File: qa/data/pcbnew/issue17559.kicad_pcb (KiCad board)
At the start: 2 copper layers, 110.5 x 93.7 mm, 6 parts, among them IC5 AD8418AWBRZ, IC6 AD8418AWBRZ

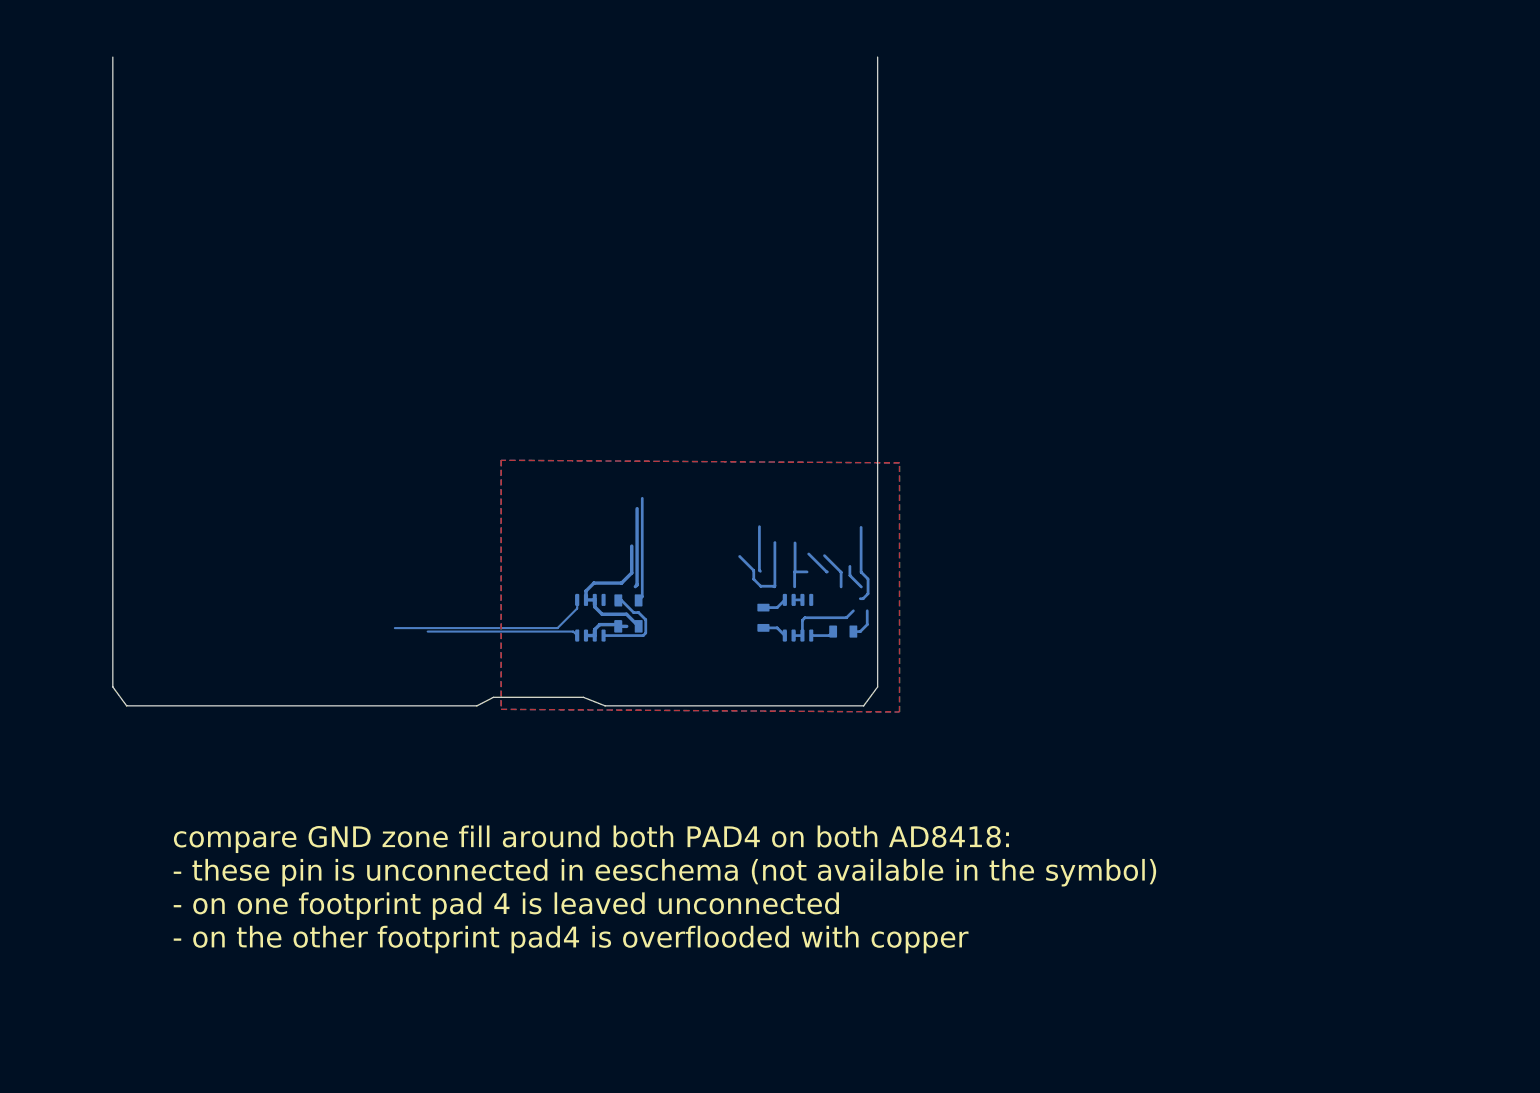
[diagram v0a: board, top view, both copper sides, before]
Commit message: feat: update kicad to 9.0.0+dfsg-1
Signed-off-by: lhdjply <lhdjply@126.com>
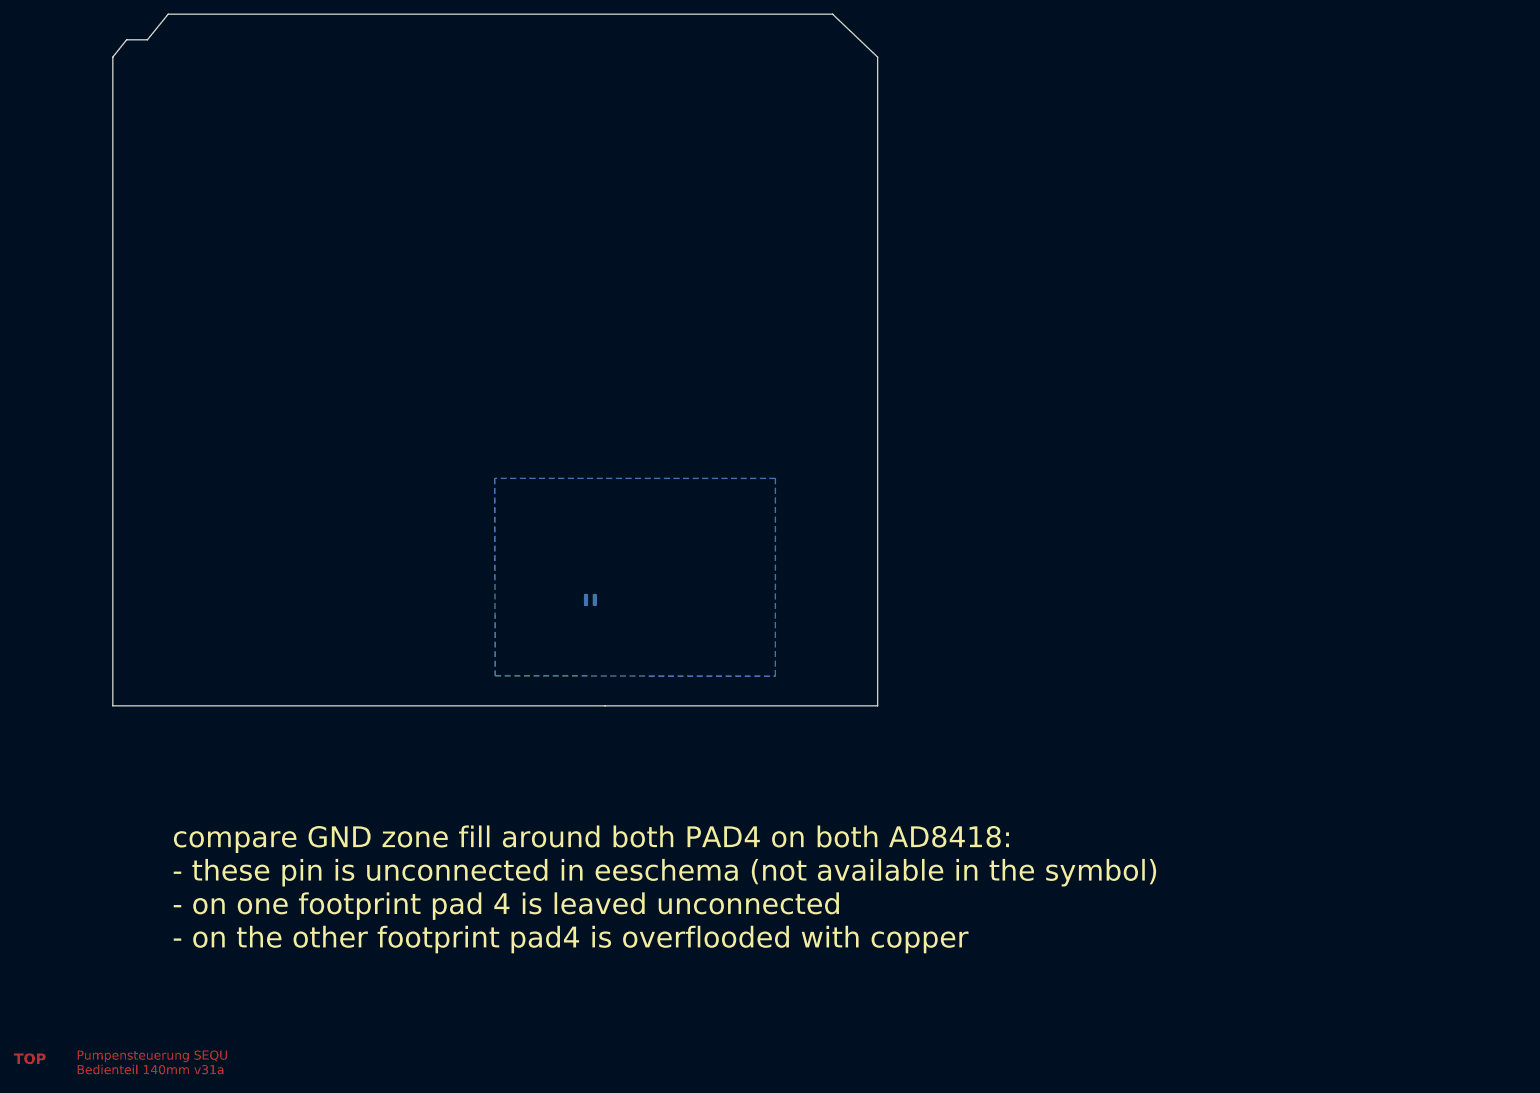
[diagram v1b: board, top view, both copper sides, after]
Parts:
- removed C12: 100nF, 0IBF_RCL:C_1206_3216Metric
- removed IC6: AD8418AWBRZ, 0IBF_IC_spezial:SO-8_3.9x4.9mm_P1.27mm_IBF
- removed R13, R29, R9: 1k, 0IBF_RCL:R_1206_3216Metric
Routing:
- net (no net): track 46.7 -> 0.00 mm
- net GND: track 41.5 -> 0.00 mm
- net Net-(IC5--in): track 28.8 -> 0.00 mm
- net Net-(IC5-+in): track 21.8 -> 0.00 mm
- net +3V3: track 18.6 -> 0.00 mm
- net ADC0_5_STROM: track 15.0 -> 0.00 mm
- net Net-(IC5-out): track 13.3 -> 0.00 mm
- net unconnected-(R9-Pad1): track 4.41 -> 0.00 mm
- net Net-(IC6--in): track 3.56 -> 0.00 mm
- net Net-(IC6-+in): track 3.56 -> 0.00 mm
- net Net-(IC6-out): track 3.41 -> 0.00 mm
- removed copper zone on F.Cu, net GND
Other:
- board size 110.5 x 93.7 mm -> 110.5 x 99.9 mm
- board text added: "Pumpensteuerung SEQU Bedienteil 140mm v31a"
- board text added: "TOP"
